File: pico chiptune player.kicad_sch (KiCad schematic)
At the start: 24 parts, among them J1 Speaker Out, J2 MicroSD, SW1 Play / Pause, SW2 Next, SW3 Previous, U1 AY-3-8910, U2 0.96"OLED_I2C, U3 PAM8302AAS

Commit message: Refactor code structure for improved readability and maintainability
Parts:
- removed C1: 10uF, Capacitor_SMD:CP_Elec_3x5.3, symbol Device:C
- removed J1: Speaker Out, Connector_PinSocket_1.27mm:PinSocket_2x01_P1.27mm_Vertical, symbol Connector:Conn_01x02_Pin
- removed R6: 10K, Resistor_SMD:R_0805_2012Metric_Pad1.20x1.40mm_HandSolder, symbol Device:R
- removed RV1: 3224W-1-103E, Potentiometer_SMD:Potentiometer_Bourns_3224W_Vertical, symbol BOURNS_3224W-1-103E:BOURNS_3224W-1-103E
- removed U3: PAM8302AAS, Package_SO:SOIC-8_3.9x4.9mm_P1.27mm, symbol Amplifier_Audio:PAM8302AAS
- added C1, C6: 10uF, Capacitor_SMD:CP_Elec_4x5.4, symbol Device:C_Polarized_Small
- added C7, C8: 100nF, Capacitor_SMD:C_0805_2012Metric_Pad1.18x1.45mm_HandSolder, symbol Device:C
- added U3: PAM8302, TModules:PAM8302A_Module, symbol terence:PAM8302
- A1: footprint Module_RaspberryPi_Pico:RaspberryPi_Pico_Common -> TMCu Module:RPi_Pico_SMD_TH; LCSC Part # C17414 -> (none)
- C2: LCSC C81348 -> (none); LCSC Part # C81348 -> C1711
- C3: LCSC C17513 -> (none); LCSC Part # C17513 -> C3348
- C4: value 10nF -> 100nF; LCSC Part # (none) -> C1710
- C5: value 10nF -> 100nF; LCSC Part # C17414 -> C1710
- J2: footprint terence:MicroSD -> Terence:MicroSD; LCSC Part # (none) -> C479742
- JP1, SW1, SW2, SW3: now left out of the parts list
- R1: LCSC Part # C17631 -> C17414
- R2: LCSC C17631 -> (none); LCSC Part # (none) -> C17634
- R3: LCSC C17414 -> (none); LCSC Part # (none) -> C17414
- R4: LCSC C12437 -> (none); LCSC Part # C12437 -> C17513
- R5: LCSC C17513 -> (none)
- R7, R8: LCSC Part # (none) -> C17513
- U2: footprint terence:0.96OLED I2C -> TModules:OLED 0.96 I2C
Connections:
- net +3.3V: now also C6.1, C7.1
- net +5V: now also C1.1, C8.1, U3.2 (VIN)
- net BC1: now also A1.11 (GPIO8); no longer A1.12 (GPIO9)
- net BDIR: now also A1.14 (GPIO10); no longer A1.11 (GPIO8)
- net GND: now also C1.2, C6.2, C7.2, C8.2, U3.1 (GND), U3.4 (A-)
- net SW_NEXT: now also A1.17 (GPIO13); no longer A1.20 (GPIO15)
- net SW_PLAY: now also A1.19 (GPIO14); no longer A1.17 (GPIO13)
- net SW_PREV: now also A1.20 (GPIO15); no longer A1.16 (GPIO12)
- net ~{RESET}: now also A1.15 (GPIO11); no longer A1.14 (GPIO10)
- net at C3.2: now also U3.5 (A+)
- net at R2.2: now also A1.16 (GPIO12); no longer A1.15 (GPIO11)
- new net SD_Amp: A1.12 (GPIO9), U3.3 (SD)
- no-connect marks 29 -> 30
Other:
- moved on the sheet: C3, R2

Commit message: sch, pcb, docs: update to Rev 0.5 native-compliant SD/OLED pinout
Remap RP2350 peripherals to their native pins: OLED SDA=GP16/SCL=GP17, SD SCK=GP18/MOSI=GP19/MISO=GP20/CS=GP21 (card detect stays GP22).

- Schematic: swap OLED SDA/SCL labels, remap SD SPI labels, move R1 pull-up back onto SD_CS; retitle to 0.5
- PCB: resync A1 pads, reroute the 5 affected nets (0 unconnected), refill zones, retitle to 0.5; DRC unchanged from Rev 0.4
- Docs: HARDWARE.md/README.md/VERSION set as Rev 0.5 SSOT with errata
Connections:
- net OLED_SCL: now also A1.22 (GPIO17); no longer A1.21 (GPIO16)
- net OLED_SDA: now also A1.21 (GPIO16); no longer A1.22 (GPIO17)
- net SD_CS: now also A1.27 (GPIO21); no longer A1.24 (GPIO18)
- net SD_MISO: now also A1.26 (GPIO20); no longer A1.27 (GPIO21)
- net SD_SCK: now also A1.24 (GPIO18); no longer A1.26 (GPIO20)
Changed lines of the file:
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@@
 	(title_block
 		(title "Pico Chiptune Player")
-		(date "2026-08-12")
-		(rev "0.2")
+		(date "2026-10-11")
+		(rev "0.5")
 		(company "MotionFxDesign")
 		(comment 1 "Terence Ang / MotionFxDesign")
@@
 		)
 	)
-	(wire
-		(pts
-			(xy 118.11 55.88) (xy 118.11 62.23)
-		)
-		(stroke
-			(width 0)
-			(type default)
+	(label "SD_CS"
+		(at 118.11 55.88 0)
+		(effects
+			(font
+				(size 1.27 1.27)
+			)
+			(justify left bottom)
 		)
 	)
@@
 		)
 	)
-	(label "SD_SCK"
+	(label "SD_MISO"
 		(at 101.6 67.31 0)
 		(effects
@@
 		)
 	)
-	(label "OLED_SCL"
+	(label "OLED_SDA"
 		(at 101.6 57.15 0)
 		(effects
@@
 		)
 	)
-	(label "SD_MISO"
+	(label "SD_CS"
 		(at 101.6 69.85 0)
 		(effects
@@
 		)
 	)
-	(label "OLED_SDA"
+	(label "OLED_SCL"
 		(at 101.6 59.69 0)
 		(effects
@@
 		)
 	)
-	(label "SD_CS"
+	(label "SD_SCK"
 		(at 120.65 62.23 0)
 		(effects

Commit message: sch, pcb, docs: dual YM2149 stereo variant (Rev 0.6)
- Add second PSG (U4) sharing DA0..7/CLOCK/~RESET/BC2, driven by
  dedicated BDIR2 (GPIO26) and BC1_2 (GPIO27) for 6 voices total
- Add right-channel passive mixer (R9-R12, C9, C10) and second
  PAM8302A amp module (U5) with decoupling (C11-C13) for stereo
- Widen board to 139.4 x 62.6 mm; autoroute with Freerouting
  (0 unconnected items, ERC 0 errors)
- Update HARDWARE.md/README.md/VERSION to Rev 0.6
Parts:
- added C10: 1uF, Capacitor_SMD:CP_Elec_3x5.4, symbol Device:C_Polarized
- added C11: 10uF, Capacitor_SMD:CP_Elec_4x5.4, symbol Device:C_Polarized_Small
- added C12, C13, C9: 100nF, Capacitor_SMD:C_0805_2012Metric_Pad1.18x1.45mm_HandSolder, symbol Device:C
- added R10, R11, R12, R9: 1k, Resistor_SMD:R_0805_2012Metric_Pad1.20x1.40mm_HandSolder, symbol Device:R
- added U4: YM2149F, Package_DIP:DIP-40_W15.24mm, symbol AY-3-8910:AY-3-8910
- added U5: PAM8302, TModules:PAM8302A_Module, symbol terence:PAM8302
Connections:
- net +5V: now also C11.1, C12.1, C13.1, U4.25 (A8), U4.28 (BC2), U4.40 (VCC), U5.2 (VIN)
- net CLOCK: now also U4.22 (CLOCK)
- net DA0: now also U4.37 (DA0)
- net DA1: now also U4.36 (DA1)
- net DA2: now also U4.35 (DA2)
- net DA3: now also U4.34 (DA3)
- net DA4: now also U4.33 (DA4)
- net DA5: now also U4.32 (DA5)
- net DA6: now also U4.31 (DA6)
- net DA7: now also U4.30 (DA7)
- net GND: now also C11.2, C12.2, C13.2, C9.2, R12.2, U4.1 (VSS), U4.24 (A9), U5.1 (GND), U5.4 (A-)
- net SD_Amp: now also U5.3 (SD)
- net ~{RESET}: now also U4.23 (~{RESET})
- net JP1_SEL: now reaches JP1.1 (A), U1.26 (~{CS/Test_2})
- net JP1_SEL: now also U4.26 (~{CS/Test_2})
- net BDIR2: now reaches A1.31 (GPIO26_ADC0)
- net BDIR2: now also U4.27 (BDIR)
- net BC1_2: now reaches A1.32 (GPIO27_ADC1)
- net BC1_2: now also U4.29 (BC1)
- new net AMP2_IN: C10.2, U5.5 (A+)
- new net ANALOG_A2: R9.1, U4.4 (ANALOG_A)
- new net ANALOG_B2: R10.1, U4.3 (ANALOG_B)
- new net ANALOG_C2: R11.1, U4.38 (ANALOG_C)
- new net MIX2: C10.1, C9.1, R10.2, R11.2, R12.1, R9.2
- no-connect marks 30 -> 49

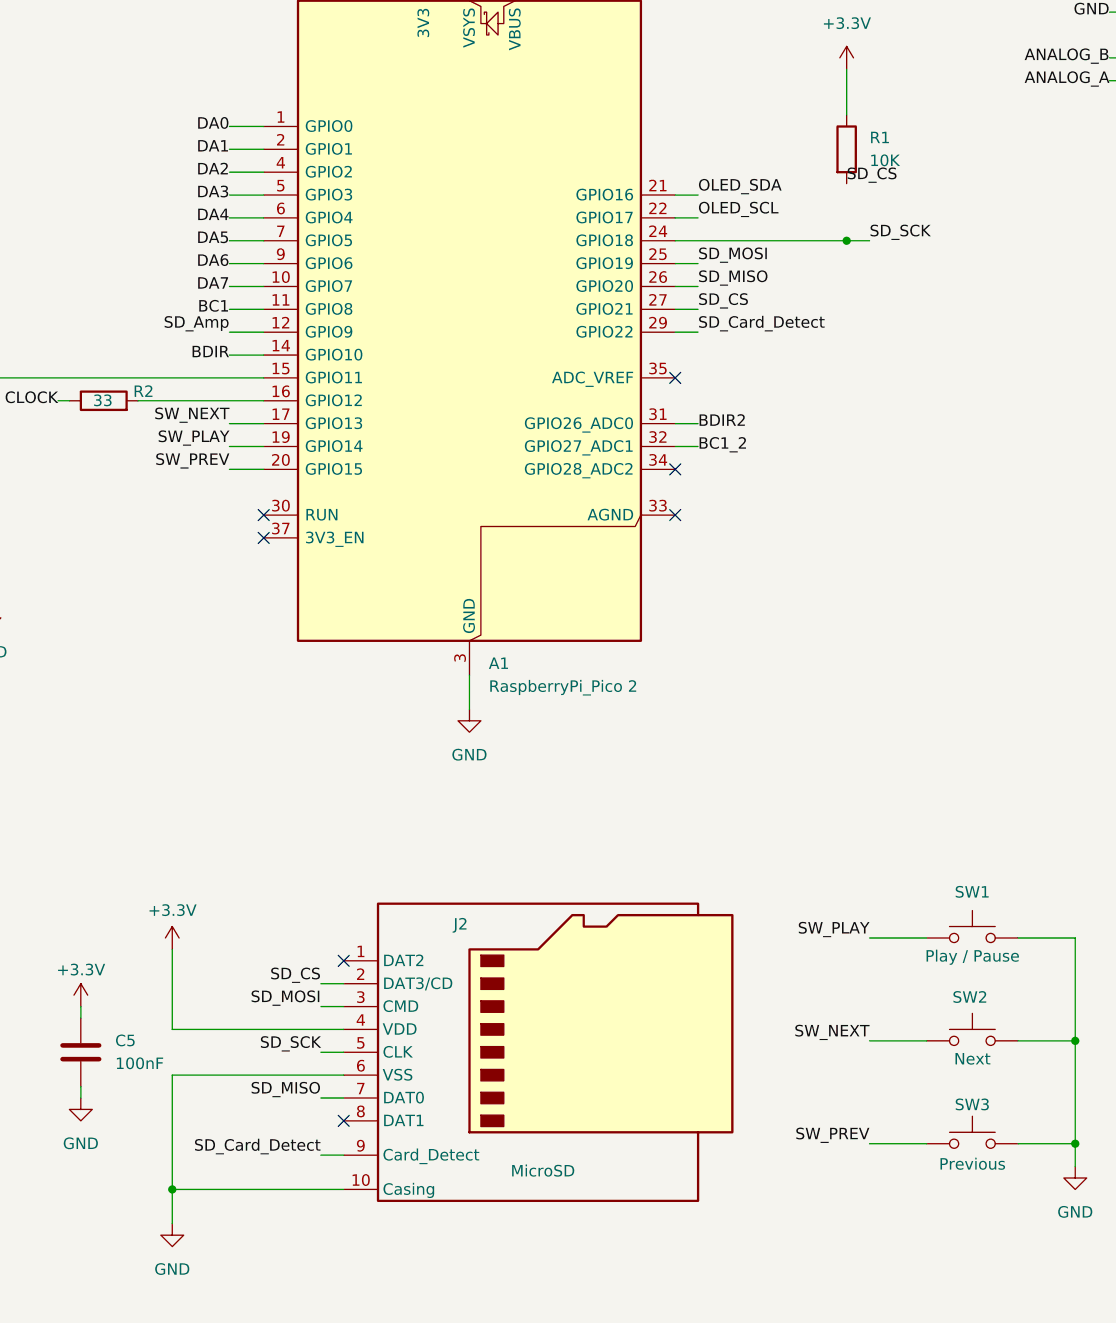
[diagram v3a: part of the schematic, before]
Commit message: microSD: switch SPI to 4-bit SDIO (Rev 0.6)
Re-map microSD socket J2 from SPI to 4-bit SDIO for the RP2350 PIO
pico_sd_card driver: SD_DAT0..DAT3 -> GPIO18..21, SD_CLK -> GPIO22,
SD_CMD -> GPIO28. Drop the dedicated card-detect switch (presence now
detected in software); R1 10k stays on DAT3. Update HARDWARE.md/README.md
pinout, BOM and revision notes. PCB rerouted: 0 unconnected, 0
shorts/clearance, 12 cosmetic DRC items; ERC clean.
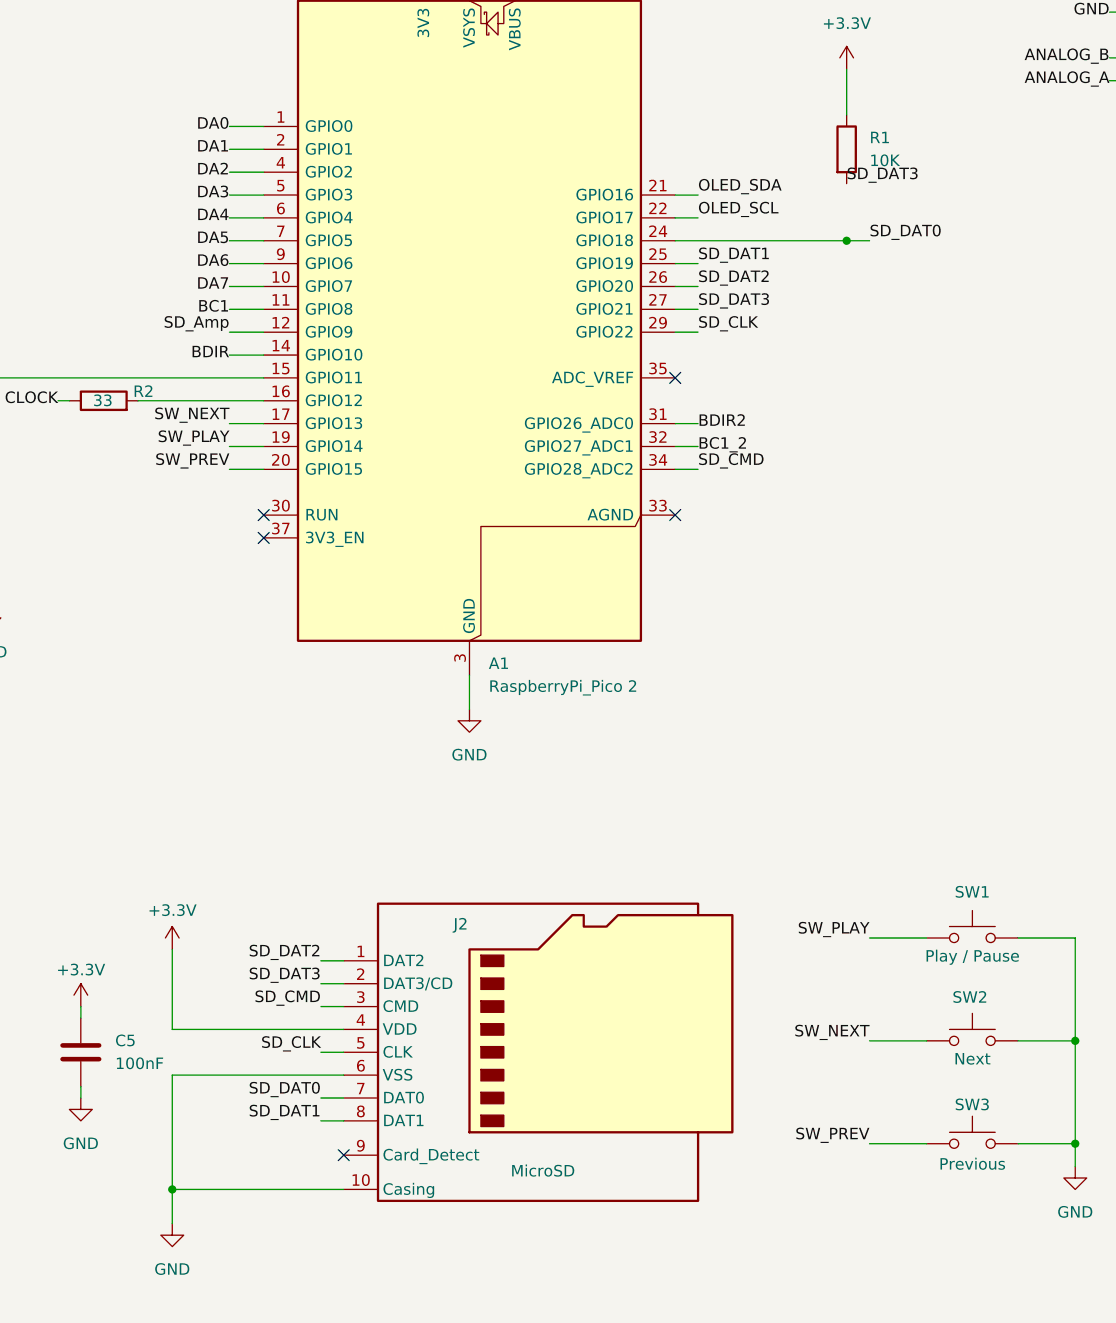
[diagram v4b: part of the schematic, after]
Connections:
- net SD_DAT2: now reaches J2.1 (DAT2)
- net SD_DAT2: now also A1.26 (GPIO20)
- net SD_DAT1: now reaches J2.8 (DAT1)
- net SD_DAT1: now also A1.25 (GPIO19)
- net SD_CMD: now reaches A1.34 (GPIO28_ADC2)
- net SD_CMD: now also J2.3 (CMD)
- net SD_CS renamed SD_DAT3
- net SD_Card_Detect: no longer names the net of J2.9 (Card_Detect)
- net SD_Card_Detect: no longer A1.29 (GPIO22)
- net SD_MISO renamed SD_DAT0
- net SD_DAT0: now also A1.24 (GPIO18); no longer A1.26 (GPIO20)
- removed net SD_MOSI: A1.25 (GPIO19), J2.3 (CMD)
- net SD_SCK renamed SD_CLK
- net SD_CLK: now also A1.29 (GPIO22); no longer A1.24 (GPIO18)
- no-connect marks 49 -> 47
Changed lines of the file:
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@@
 	)
 	(no_connect
-		(at 99.06 87.63)
-	)
-	(no_connect
 		(at 149.86 82.55)
 	)
@@
 	)
 	(no_connect
-		(at 62.23 160.02)
-	)
-	(no_connect
 		(at 149.86 52.07)
 	)
@@
 	)
 	(no_connect
-		(at 62.23 142.24)
-	)
-	(no_connect
 		(at 236.22 118.11)
 	)
@@
 	(wire
 		(pts
-			(xy 59.69 163.83) (xy 62.23 163.83)
-		)
-		(stroke
-			(width 0)
-			(type default)
-		)
-	)
-	(wire
-		(pts
 			(xy 186.69 27.94) (xy 186.69 36.83)
 		)
@@
 		)
 	)
-	(label "SD_CS"
+	(label "SD_DAT3"
 		(at 118.11 55.88 0)
 		(effects
@@
 		)
 	)
-	(label "SD_MISO"
+	(label "SD_DAT2"
 		(at 101.6 67.31 0)
 		(effects
@@
 		)
 	)
-	(label "SD_CS"
+	(label "SD_DAT3"
 		(at 59.69 144.78 180)
 		(effects
@@
 		)
 	)
-	(label "SD_MISO"
+	(label "SD_DAT0"
 		(at 59.69 157.48 180)
 		(effects
@@
 		)
 	)
-	(label "SD_MOSI"
+	(label "SD_DAT1"
 		(at 101.6 64.77 0)
 		(effects
@@
 		)
 	)
-	(label "SD_SCK"
+	(label "SD_CLK"
 		(at 59.69 152.4 180)
 		(effects
@@
 		)
 	)
-	(label "SD_MOSI"
+	(label "SD_CMD"
 		(at 59.69 147.32 180)
 		(effects
@@
 		)
 	)
-	(label "SD_CS"
+	(label "SD_DAT3"
 		(at 101.6 69.85 0)
 		(effects
@@
 		)
 	)
-	(label "SD_Card_Detect"
-		(at 59.69 163.83 180)
-		(effects
-			(font
-				(size 1.27 1.27)
-			)
-			(justify right bottom)
-		)
-	)
 	(label "SW_PREV"
 		(at 120.65 162.56 180)
@@
 		)
 	)
-	(label "SD_Card_Detect"
+	(label "SD_CLK"
 		(at 101.6 72.39 0)
 		(effects
@@
 		)
 	)
-	(label "SD_SCK"
+	(label "SD_DAT0"
 		(at 120.65 62.23 0)
 		(effects
@@
 		)
 	)
+	(wire
+		(pts
+			(xy 99.06 87.63) (xy 101.6 87.63)
+		)
+		(stroke
+			(width 0)
+			(type default)
+		)
+	)
+	(label "SD_CMD"
+		(at 101.6 87.63 0)
+		(effects
+			(font
+				(size 1.27 1.27)
+			)
+			(justify left bottom)
+		)
+	)
+	(wire
+		(pts
+			(xy 59.69 160.02) (xy 62.23 160.02)
+		)
+		(stroke
+			(width 0)
+			(type default)
+		)
+	)
+	(label "SD_DAT1"
+		(at 59.69 160.02 180)
+		(effects
+			(font
+				(size 1.27 1.27)
+			)
+			(justify right bottom)
+		)
+	)
+	(wire
+		(pts
+			(xy 59.69 142.24) (xy 62.23 142.24)
+		)
+		(stroke
+			(width 0)
+			(type default)
+		)
+	)
+	(label "SD_DAT2"
+		(at 59.69 142.24 180)
+		(effects
+			(font
+				(size 1.27 1.27)
+			)
+			(justify right bottom)
+		)
+	)
+	(no_connect
+		(at 62.23 163.83)
+	)
 	(sheet_instances

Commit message: Refactor code structure for improved readability and maintainability
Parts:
- removed U3, U5: PAM8302, TModules:PAM8302A_Module, symbol terence:PAM8302
- added C14, C16: 1uF, Capacitor_SMD:C_0805_2012Metric_Pad1.18x1.45mm_HandSolder, symbol Device:C
- added C15: 10uF, Capacitor_SMD:CP_Elec_4x5.4, symbol Device:C_Polarized
- added J3: Speaker_L, Connector_JST:JST_PH_B2B-PH-K_1x02_P2.00mm_Vertical, symbol Connector_Generic:Conn_01x02
- added J4: Speaker_R, Connector_JST:JST_PH_B2B-PH-K_1x02_P2.00mm_Vertical, symbol Connector_Generic:Conn_01x02
- added R13: 10K, Resistor_SMD:R_0805_2012Metric_Pad1.20x1.40mm_HandSolder, symbol Device:R
- added U3: PAM8403, Package_SO:SOIC-16_3.9x9.9mm_P1.27mm, symbol Amplifier_Audio:PAM8403D
- C10: footprint Capacitor_SMD:CP_Elec_3x5.4 -> Capacitor_SMD:C_0805_2012Metric_Pad1.18x1.45mm_HandSolder; symbol Device:C_Polarized -> Device:C; LCSC Part # (none) -> C28323
- C13: value 100nF -> 1uF; LCSC Part # (none) -> C28323
- C3: footprint Capacitor_SMD:CP_Elec_3x5.4 -> Capacitor_SMD:C_0805_2012Metric_Pad1.18x1.45mm_HandSolder; symbol Device:C_Polarized -> Device:C; LCSC Part # C3348 -> C28323
- C8: value 100nF -> 1uF; LCSC Part # C1710 -> C28323
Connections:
- net +5V: now also C14.1, C15.1, U3.13 (PVDD), U3.4 (PVDD), U3.6 (VDD)
- net GND: now also C14.2, C15.2, C16.2, R13.2, U3.11 (GND), U3.15 (PGND), U3.2 (PGND)
- net SD_Amp: now also R13.1, U3.12 (~{SHDN}), U3.5 (~{MUTE})
- net AMP_INL: now reaches C3.2
- net AMP_INL: now also U3.7 (INL)
- net AMP2_IN renamed AMP_INR
- net AMP_INR: now also U3.10 (INR)
- new net AMP_VREF: C16.1, U3.8 (VREF)
- new net SPK_L+: J3.1 (Pin_1), U3.1 (LOUT+)
- new net SPK_L-: J3.2 (Pin_2), U3.3 (LOUT-)
- new net SPK_R+: J4.1 (Pin_1), U3.16 (ROUT+)
- new net SPK_R-: J4.2 (Pin_2), U3.14 (ROUT-)
- no-connect marks 47 -> 44
